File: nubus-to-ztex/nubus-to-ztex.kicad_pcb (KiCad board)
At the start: 4 copper layers, 161.6 x 100 mm, 98 parts, among them J1 87832-1420 (2x7 M 2mm), J2 47219-2001 (micro-sd), J3 Conn_01x06_Male, J4 0850030567 (DIN 41612C 3x32 p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, J5 10029449-111RLF (HDMI A), J6 105017-0001 (USB micro-B), J7 640456-3 (Fan), J8 SMH-108-02-L-D (Pmod 2x8 F), U1 74LVT125PW,118, U10 SN65220DBV, U11 TPS2051CDBV, U13 SN74CB3T3245PWR, U14 SN74CB3T3245PWR, U15 SN74CB3T3245PWR, U2 74LVT125PW,118, U3 74LVT125PW,118, U5 74LVT245BPW,118, U6 74LVT245BPW,118, U7 74LVT245BPW,118, U8 74LVT245BPW,118, U9 TPD12S016PWR

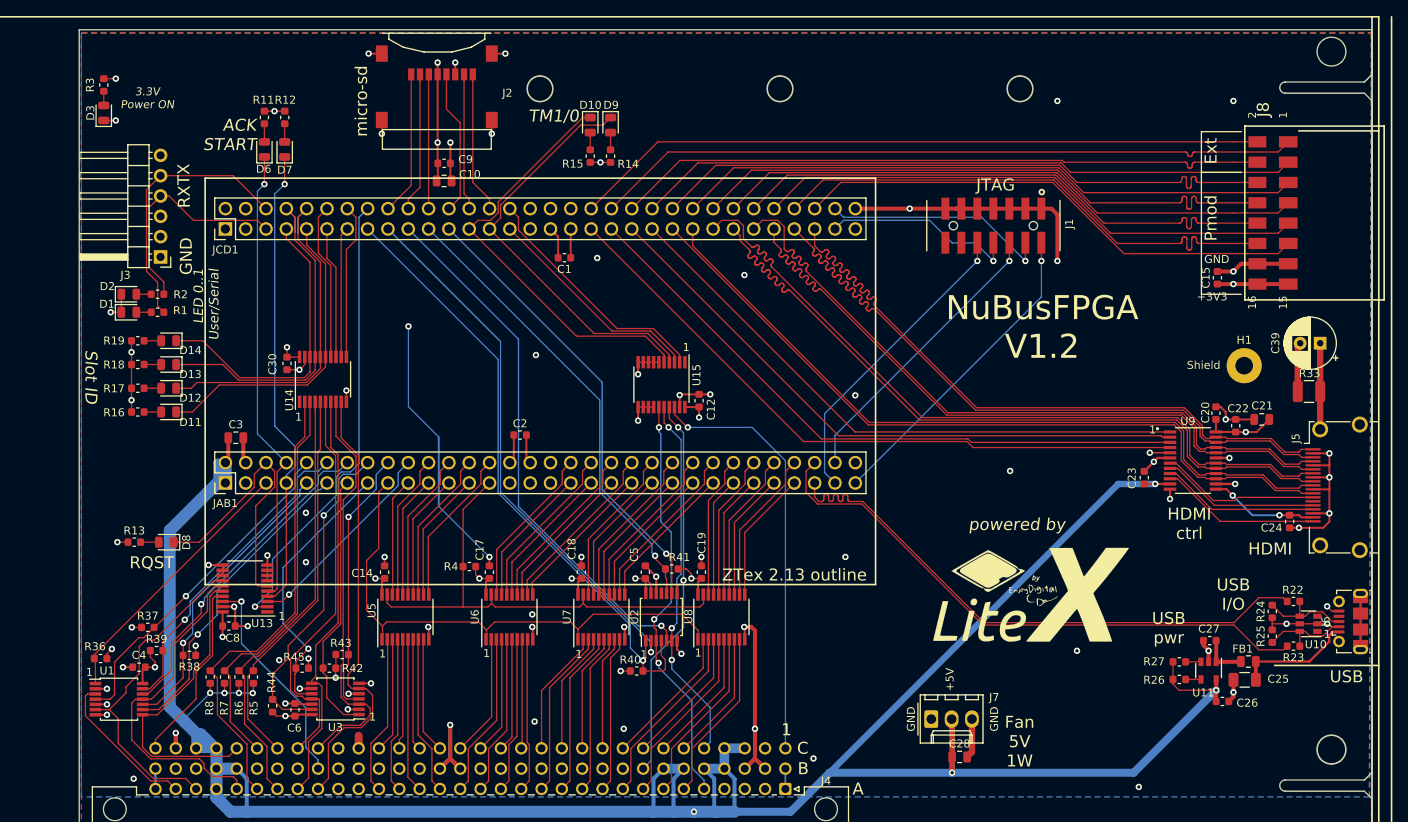
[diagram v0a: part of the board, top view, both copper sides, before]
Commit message: more THT->SMT, lexx expensive parts/assembly (?)
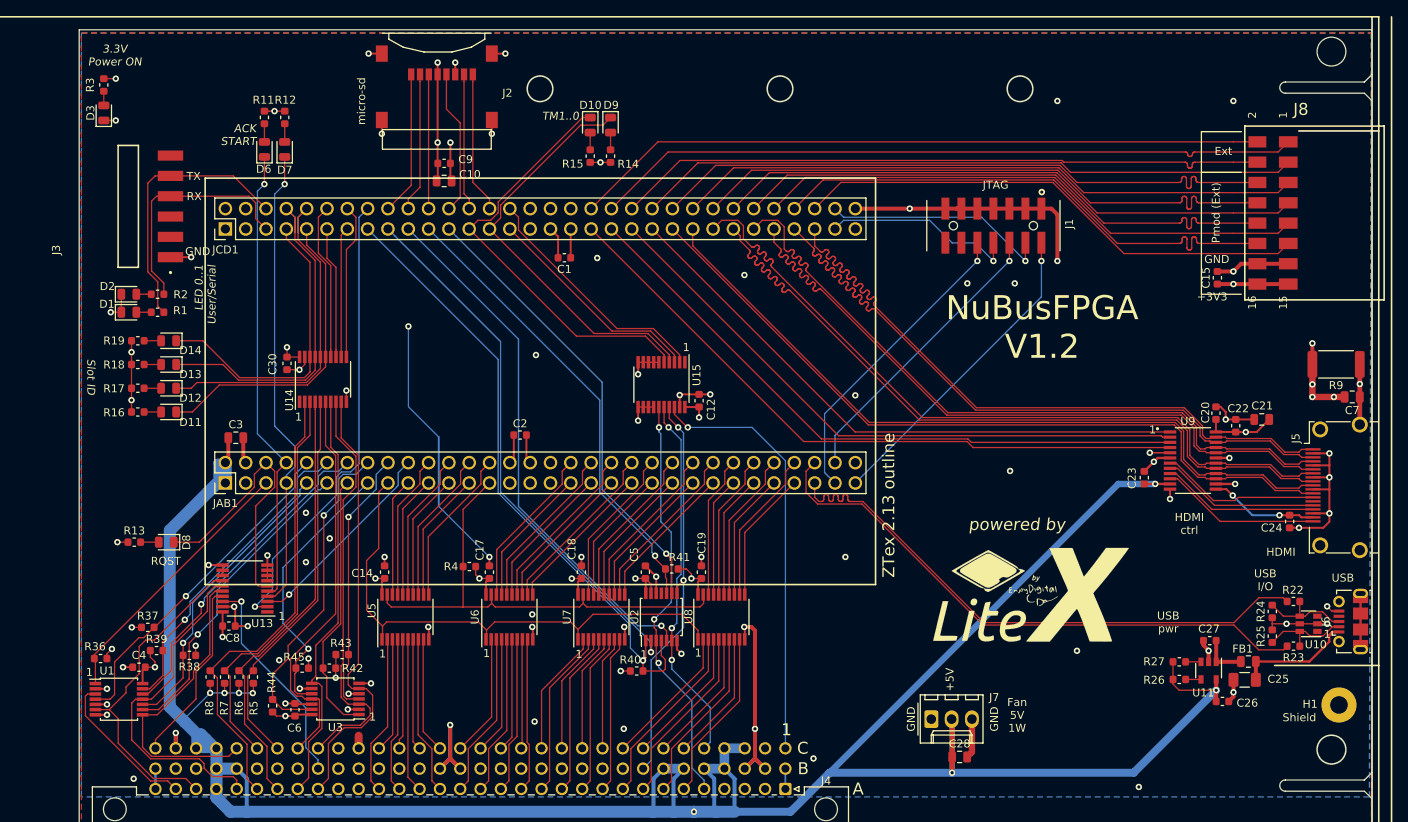
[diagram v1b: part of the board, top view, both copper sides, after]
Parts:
- removed C39: 1uF 250V Radial 6.3x2.5, Capacitor_THT:CP_Radial_D6.3mm_P2.50mm
- removed R33: 1M 1210, Resistor_SMD:R_1210_3225Metric
- added C7: 10nF 1kV 0805, Capacitor_SMD:C_0805_2012Metric, F.Cu at (270.9, 51.0)
- added R9: 1M 500V 2512, Resistor_SMD:R_2512_6332Metric, F.Cu at (268.8, 46.9)
- J3: footprint For_SeeedStudio:PinHeader_1x06_P2.54mm_Horizontal_For_SeeedStudio -> For_SeeedStudio:SAMTEC_TSM-106-01-L-SH
- J4: value 0850030567 (DIN 41612C 3x32 pins) -> 09031966921 (DIN 41612C 3x32 pins)
- moved H1 44.0 mm to (269.2, 89.5)
- moved J3 7.50 mm to (117.9, 27.2), turned to 90 degrees
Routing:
- net GND: track 1487.9 -> 1528.8 mm, vias 74 -> 82
- net SHIELD: track 81.7 -> 71.1 mm, vias 0 -> 1
- net LED1: track 28.7 -> 29.7 mm
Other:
- board text added: "Pmod (Ext)"
- board text added: "TM1..0"
- board text removed: "Pmod"
- board text removed: "TM1/0"

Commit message: minor cleanups
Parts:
- D1, D2: value RED Led -> RED Led 0805
- D10, D6, D7, D8, D9: value YELLOW Led -> YELLOW Led 0805
- D11, D12, D13, D14: value GREEN Led -> GREEN Led 0805
- D3: value BLUE Led -> BLUE Led 0805

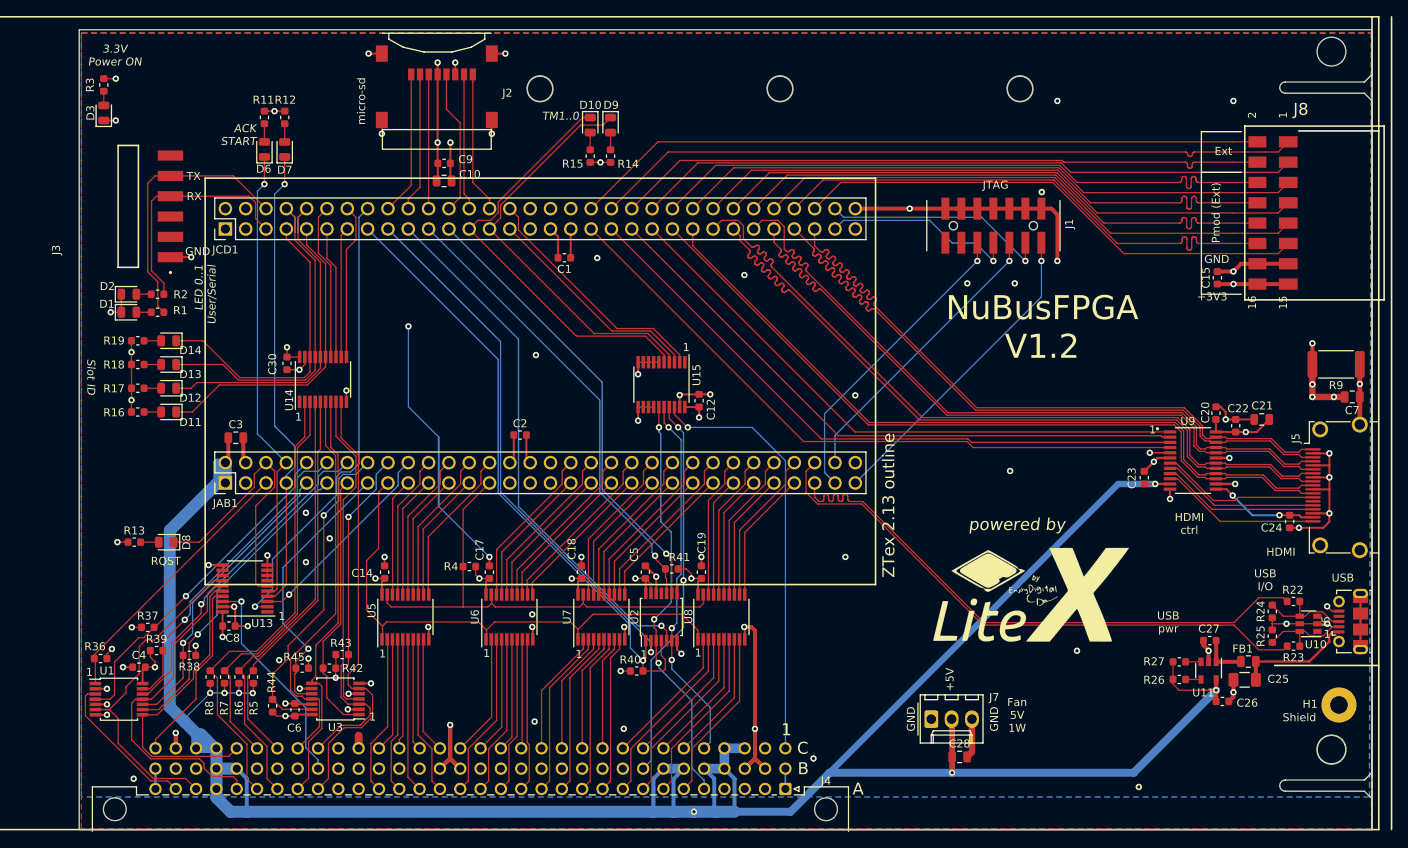
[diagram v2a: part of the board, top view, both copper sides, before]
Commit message: BoM, power plane, serial back to THT, ...
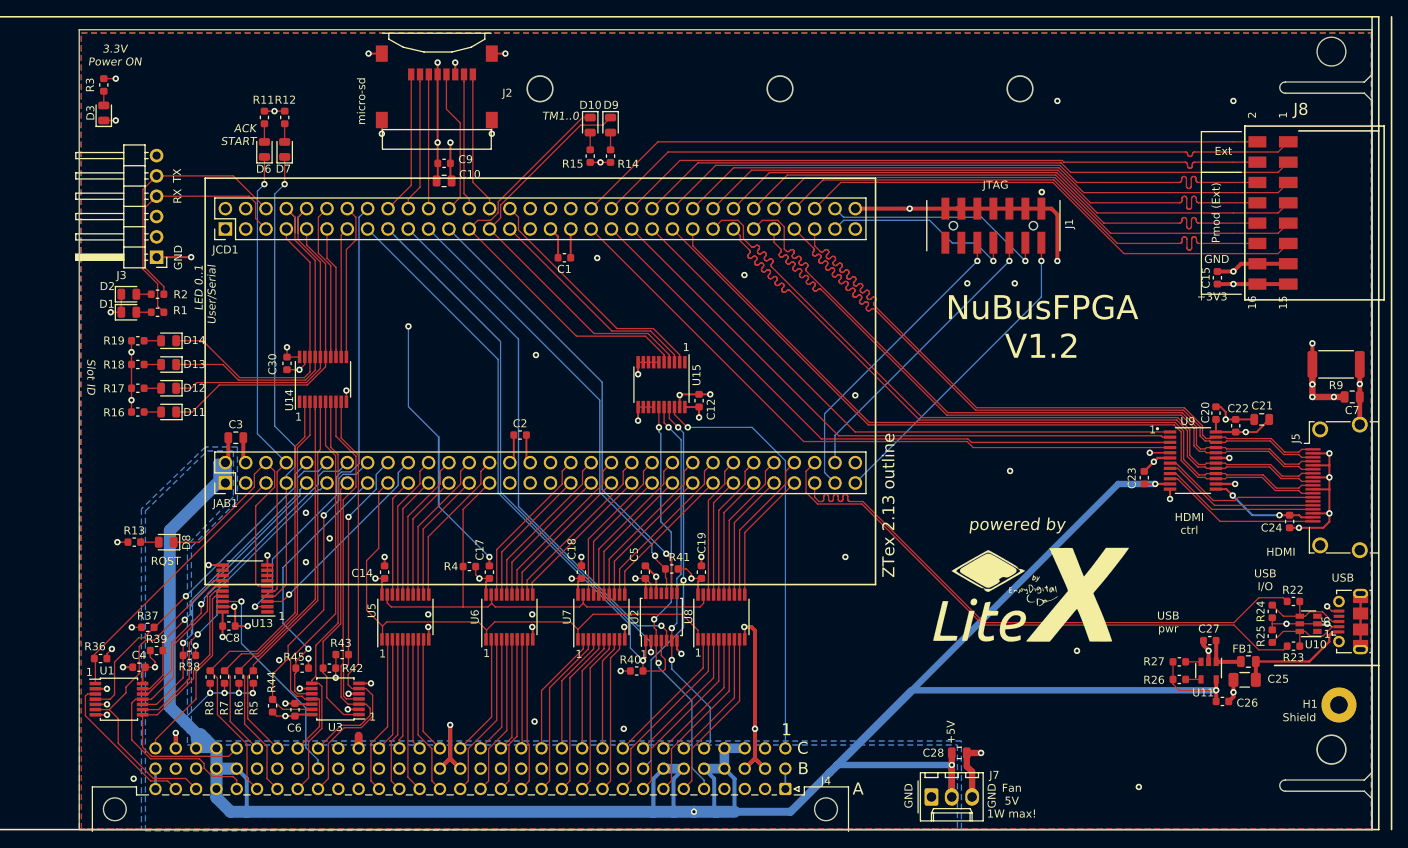
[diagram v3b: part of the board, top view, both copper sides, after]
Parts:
- J3: footprint For_SeeedStudio:SAMTEC_TSM-106-01-L-SH -> For_SeeedStudio:PinHeader_1x06_P2.54mm_Horizontal_For_SeeedStudio
- J4: value 09031966921 (DIN 41612C 3x32 pins) -> 85003-0567 (DIN 41612C 3x32 pins)
- moved J7 9.73 mm to (218.3, 101.0)
- moved J3 7.27 mm to (121.4, 33.5), turned to 180 degrees
- moved C28 0.50 mm to (221.7, 95.5)
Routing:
- net GND: track 1528.8 -> 1537.0 mm, vias 82 -> 83
- net +5V: track 342.7 -> 338.5 mm
- net LED1: track 29.7 -> 30.3 mm
- added copper zone on B.Cu, net +5V
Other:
- board text added: "Fan 5V 1W max!"
- board text removed: "Fan 5V 1W"

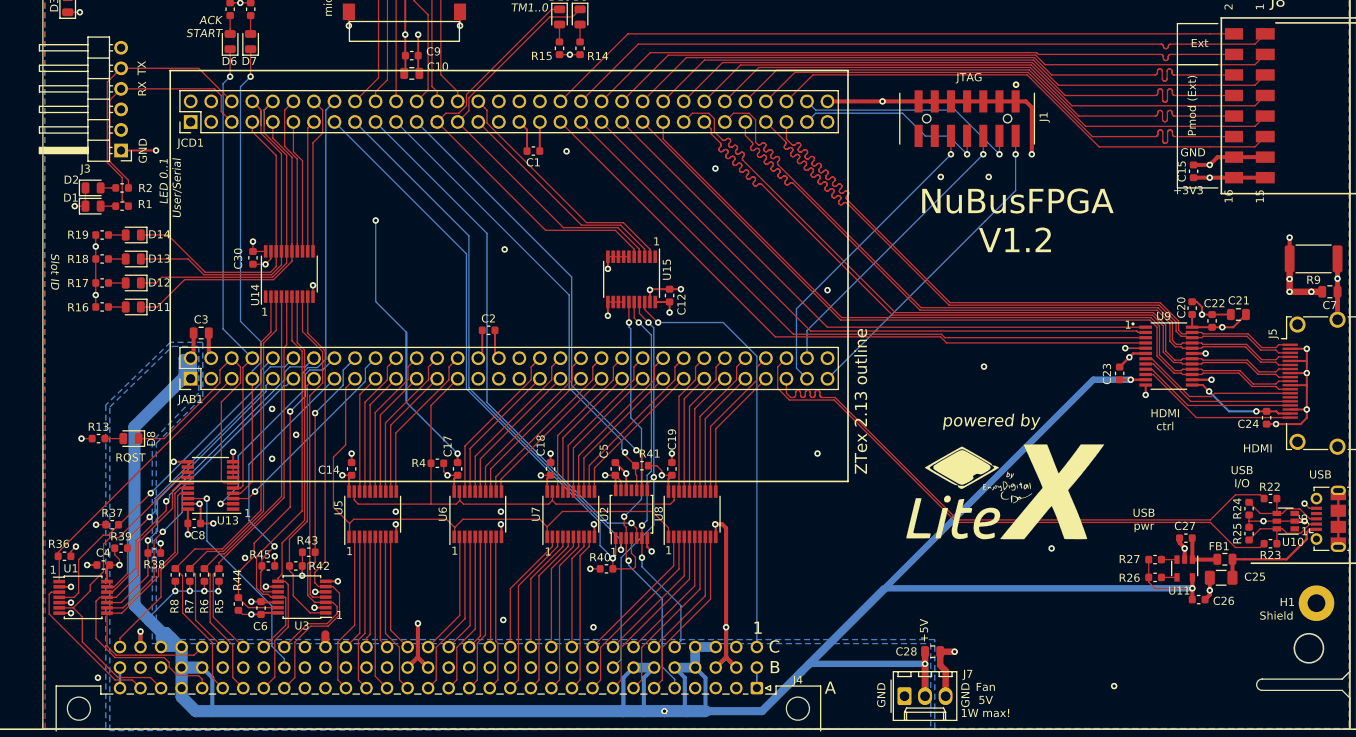
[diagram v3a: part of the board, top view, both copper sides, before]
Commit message: Smaller via, greater power/gnd clearance
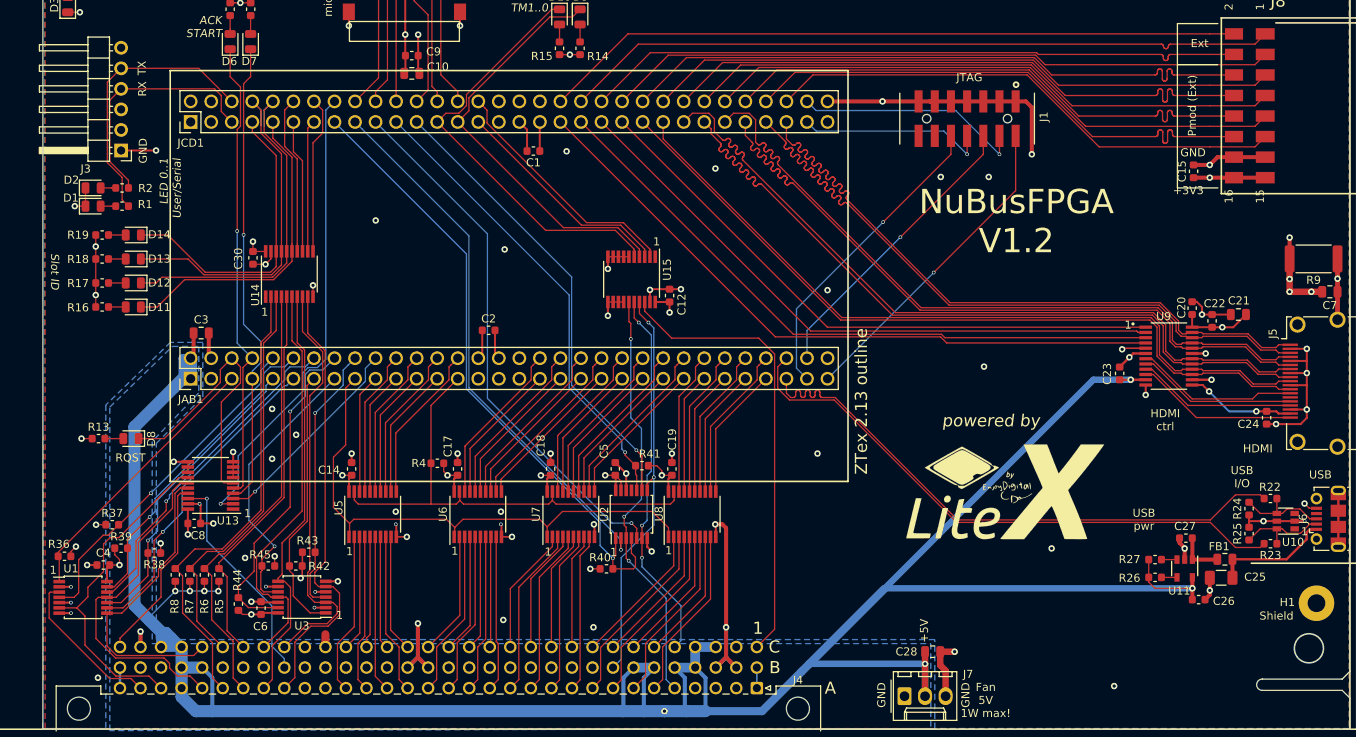
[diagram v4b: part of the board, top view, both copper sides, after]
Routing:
- net +3V3: track 670.8 -> 620.7 mm
- net GND: track 1537.0 -> 1497.4 mm, vias 83 -> 85
- net ~RESET_5V: track 53.1 -> 56.5 mm, vias 1 -> 0
- net FPGA_JTAG_TDO: track 24.6 -> 23.7 mm
- net ~ID0_5V: track 48.6 -> 48.0 mm
- net ~ACK_5V: track 42.3 -> 41.8 mm
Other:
- net class Default: via_dia 0.8 -> 0.45; via_drill 0.4 -> 0.3
- net class GND added: clearance 0.2, trace_width 0.2, via_dia 0.8, via_drill 0.4
- net class Power added: clearance 0.2, trace_width 0.2, via_dia 0.8, via_drill 0.4
- net class Shielding: clearance 0.2 -> 0.25; trace_width 0.1524 -> 0.25

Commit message: update
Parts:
- added C11: 100nF, Capacitor_SMD:C_0603_1608Metric, F.Cu at (173.1, 20.7)
- added C13: 10nF, Capacitor_SMD:C_0603_1608Metric, F.Cu at (171.1, 20.7)
- added X1: ECS-2520MV-xxx-xx, Oscillator:Oscillator_SMD_ECS_2520MV-xxx-xx-4Pin_2.5x2.0mm, F.Cu at (168.1, 20.8)
- R8: value 10k -> 27
- moved R8 73.5 mm to (166.4, 23.2), turned to 0 degrees
- moved D9 7.22 mm to (173.7, 11.3)
- moved R14 7.22 mm to (173.7, 15.2)
- moved D10 7.22 mm to (171.2, 11.3)
- moved R15 7.22 mm to (171.2, 15.2)
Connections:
- D14 pad 1: ~ID3_3V3 -> GND
- JCD1 pad 30: ~RESET_3V3 -> CLK_54_000
- JCD1 pad 7: ~ID3_3V3 -> ~RESET_3V3
- R8 pad 1: ~ID3_5V -> CLK_54_000
- R8 pad 2: +5V -> Net-(R8-Pad2)
- U14 pad 18: ~ID3_3V3 -> GND
- U14 pad 2: ~ID3_5V -> GND
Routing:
- net ~ID3_5V: track 57.7 -> 0.00 mm
- net ~ID3_3V3: track 38.0 -> 0.00 mm
- net ~RESET_3V3: track 30.7 -> 60.6 mm, vias 0 -> 1
- net GND: track 1497.4 -> 1526.5 mm, vias 85 -> 88
- net +3V3: track 620.7 -> 634.7 mm, vias 29 -> 30
- net PMOD-5: track 66.6 -> 76.2 mm
- net PMOD-6: track 64.8 -> 74.4 mm
- net PMOD-8: track 69.3 -> 78.2 mm
- net PMOD-7: track 70.4 -> 79.2 mm
- net PMOD-10: track 73.8 -> 80.6 mm
- net PMOD-9: track 75.6 -> 82.3 mm
- net PMOD-11: track 79.8 -> 85.0 mm
- net PMOD-12: track 78.4 -> 83.6 mm
- net CLK_54_000: track 0.00 -> 4.21 mm
- net ~TM0_3V3: track 51.7 -> 55.8 mm
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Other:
- outline, holes or cut-outs redrawn

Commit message: some BoM optimization
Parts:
- C25: value 100uF 1206 (officially 150 uF ? could be >= 100 uF or even less, probably) -> 100uF 1206 (officially 150 uF ? could be >= 100 uF or even less probably)
- D1, D2: value RED Led 0805 -> RED Led 0603; footprint LED_SMD:LED_0805_2012Metric -> LED_SMD:LED_0603_1608Metric
- D10, D6, D7, D8, D9: value YELLOW Led 0805 -> YELLOW Led 0603; footprint LED_SMD:LED_0805_2012Metric -> LED_SMD:LED_0603_1608Metric
- D11, D12, D13, D14: value GREEN Led 0805 -> GREEN Led 0603; footprint LED_SMD:LED_0805_2012Metric -> LED_SMD:LED_0603_1608Metric
- D3: value BLUE Led 0805 -> BLUE Led 0603; footprint LED_SMD:LED_0805_2012Metric -> LED_SMD:LED_0603_1608Metric
- J1: value 87832-1420 (2x7 M 2mm) -> 87831-1420 (2x7 M 2mm); footprint For_SeeedStudio:MOLEX_87832-1420 -> For_SeeedStudio:PinHeader_2x07_P2.00mm_Vertical_For_SeeedStudio
- J8: value SMH-108-02-L-D (Pmod 2x8 F) -> A2541HWR-2x8P (Pmod 2x8 F); footprint For_SeeedStudio:SAMTEC-SMH-108-02-X-D -> For_SeeedStudio:PinSocket_2x08_P2.54mm_Horizontal_ForSeeedStudio
- R1, R11, R12, R13, R14, R15, R16, R17, R18, R19, R2, R3: value 590 -> 560
- R9: value 1M 500V 2512 -> 1M 500V 1206; footprint Resistor_SMD:R_2512_6332Metric -> Resistor_SMD:R_1206_3216Metric
- X1: value ECS-2520MV-xxx-xx -> ASE-xxxMHz; footprint Oscillator:Oscillator_SMD_ECS_2520MV-xxx-xx-4Pin_2.5x2.0mm -> Oscillator:Oscillator_SMD_Abracon_ASE-4Pin_3.2x2.5mm
- moved J8 11.4 mm to (263.0, 36.9), turned to 180 degrees
- moved J1 5.41 mm to (231.1, 27.7)
- moved C15 3.85 mm to (257.9, 36.1)
- moved R9 1.50 mm to (270.3, 46.9)
- moved C11 0.52 mm to (173.6, 20.6)
- moved C13 0.52 mm to (171.6, 20.6)
- moved R8 0.35 mm to (166.4, 23.6)
- moved X1 0.28 mm to (168.3, 20.5), turned to 180 degrees
- moved D1 0.15 mm to (117.8, 40.4)
- moved D2 0.15 mm to (117.8, 38.2)
- moved D8 0.15 mm to (122.8, 69.2)
- moved D3 0.15 mm to (114.8, 15.7)
- moved D10 0.15 mm to (171.2, 11.1)
- moved D6 0.15 mm to (134.9, 20.2)
- moved D7 0.15 mm to (137.4, 20.2)
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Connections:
- J8 pad 1: PMOD-16 -> +3V3
- J8 pad 10: PMOD-7 -> PMOD-910+
- J8 pad 11: PMOD-6 -> PMOD-1112-
- J8 pad 12: PMOD-5 -> PMOD-1112+
- J8 pad 13: GND -> PMOD-1314-
- J8 pad 14: GND -> PMOD-1314+
- J8 pad 15: +3V3 -> PMOD-1516-
- J8 pad 16: +3V3 -> PMOD-1516+
- J8 pad 2: PMOD-15 -> +3V3
- J8 pad 3: PMOD-14 -> GND
- J8 pad 4: PMOD-13 -> GND
- J8 pad 5: PMOD-12 -> PMOD-56-
- J8 pad 6: PMOD-11 -> PMOD-56+
- J8 pad 7: PMOD-10 -> PMOD-78-
- J8 pad 8: PMOD-9 -> PMOD-78+
- J8 pad 9: PMOD-8 -> PMOD-910-
- JCD1 pad 38: PMOD-15 -> PMOD-1516-
- JCD1 pad 40: PMOD-16 -> PMOD-1516+
- JCD1 pad 42: PMOD-13 -> PMOD-1314-
- JCD1 pad 44: PMOD-14 -> PMOD-1314+
- JCD1 pad 46: PMOD-11 -> PMOD-1112-
- JCD1 pad 48: PMOD-12 -> PMOD-1112+
- JCD1 pad 50: PMOD-9 -> PMOD-910-
- JCD1 pad 52: PMOD-10 -> PMOD-910+
- JCD1 pad 54: PMOD-7 -> PMOD-78-
- JCD1 pad 56: PMOD-8 -> PMOD-78+
- JCD1 pad 58: PMOD-5 -> PMOD-56-
- JCD1 pad 60: PMOD-6 -> PMOD-56+
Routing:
- net PMOD-1112-: track 0.00 -> 100.2 mm
- net PMOD-1112+: track 0.00 -> 98.9 mm
- net PMOD-1314+: track 0.00 -> 98.1 mm
- net PMOD-910-: track 0.00 -> 97.6 mm
- net PMOD-1314-: track 0.00 -> 97.3 mm
- net PMOD-910+: track 0.00 -> 95.8 mm
- net PMOD-78-: track 0.00 -> 94.5 mm
- net PMOD-1516+: track 0.00 -> 94.2 mm
- net PMOD-78+: track 0.00 -> 93.4 mm
- net PMOD-1516-: track 0.00 -> 92.3 mm
- net PMOD-56-: track 0.00 -> 91.5 mm
- net PMOD-56+: track 0.00 -> 89.6 mm
- net PMOD-16: track 88.1 -> 0.00 mm
- net PMOD-15: track 86.7 -> 0.00 mm
- net PMOD-11: track 85.0 -> 0.00 mm
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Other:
- board text removed: "NuBusFPGA V1.2"
